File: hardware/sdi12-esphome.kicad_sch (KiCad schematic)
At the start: 24 parts, among them J1 SDI-12 A, J2 SDI-12 B, J3 SDI-12 C, J4 SDI-12 D, J5 Grounding, Q1 2N7002, U1 ESP32_NODEMCU, U2 74LVC1G125, U3 MCP1661

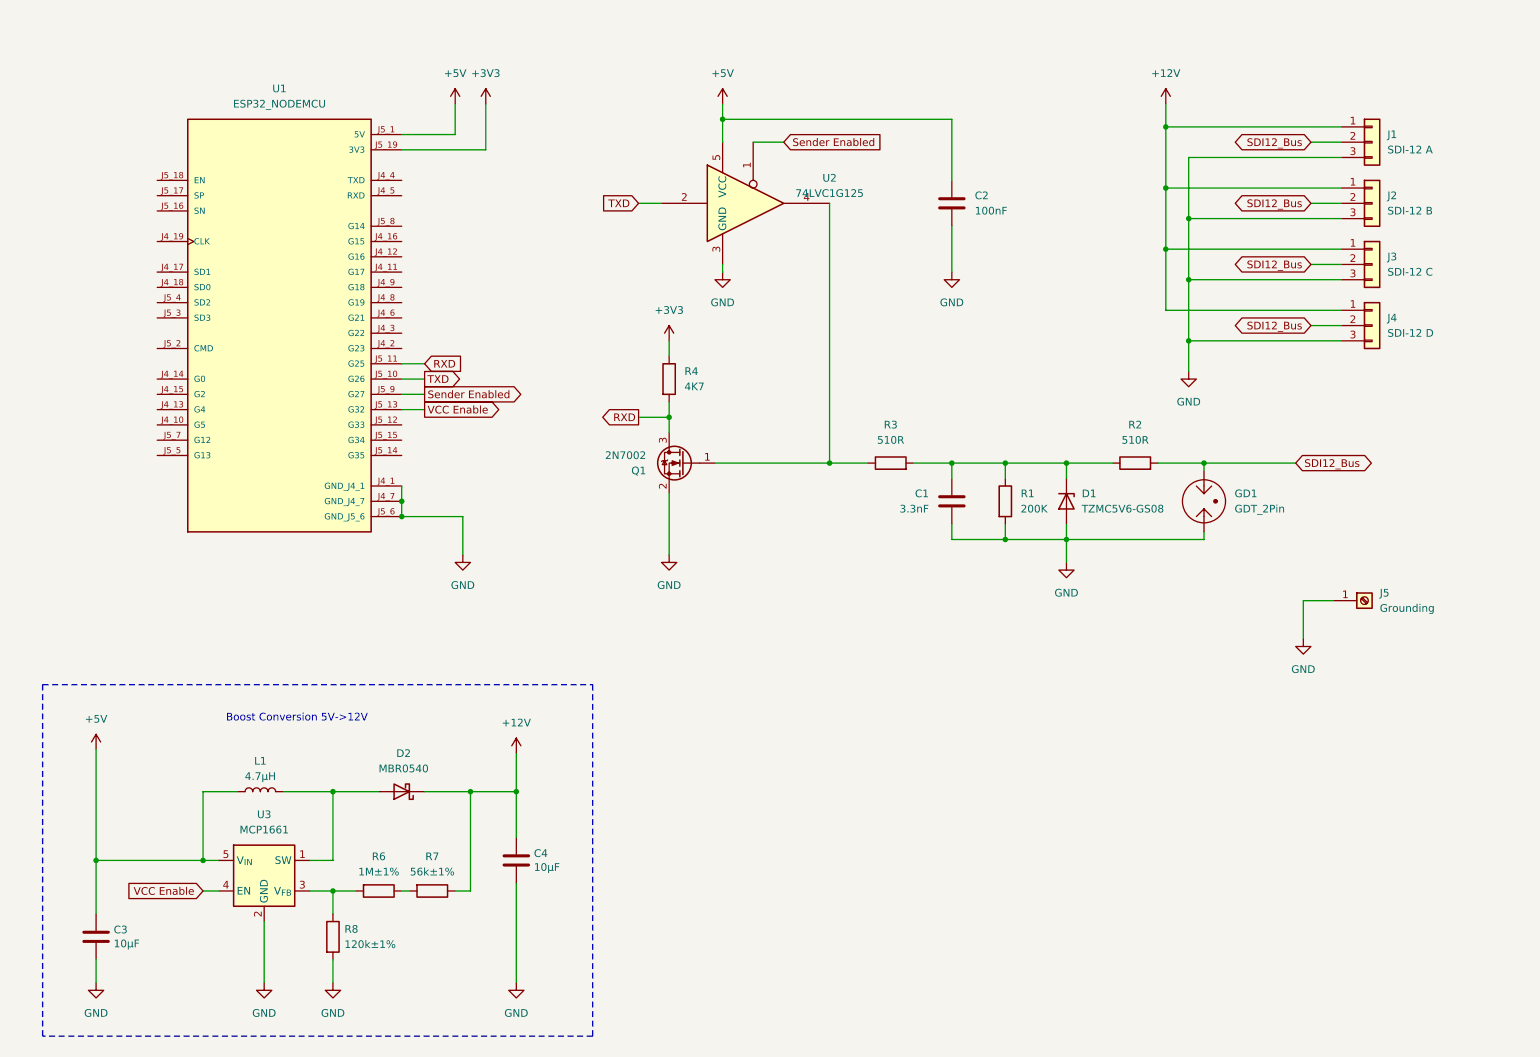
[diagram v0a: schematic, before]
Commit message: Schematic: Add additional GPIO and Rain Gauge ports, re-arrange schematic elements
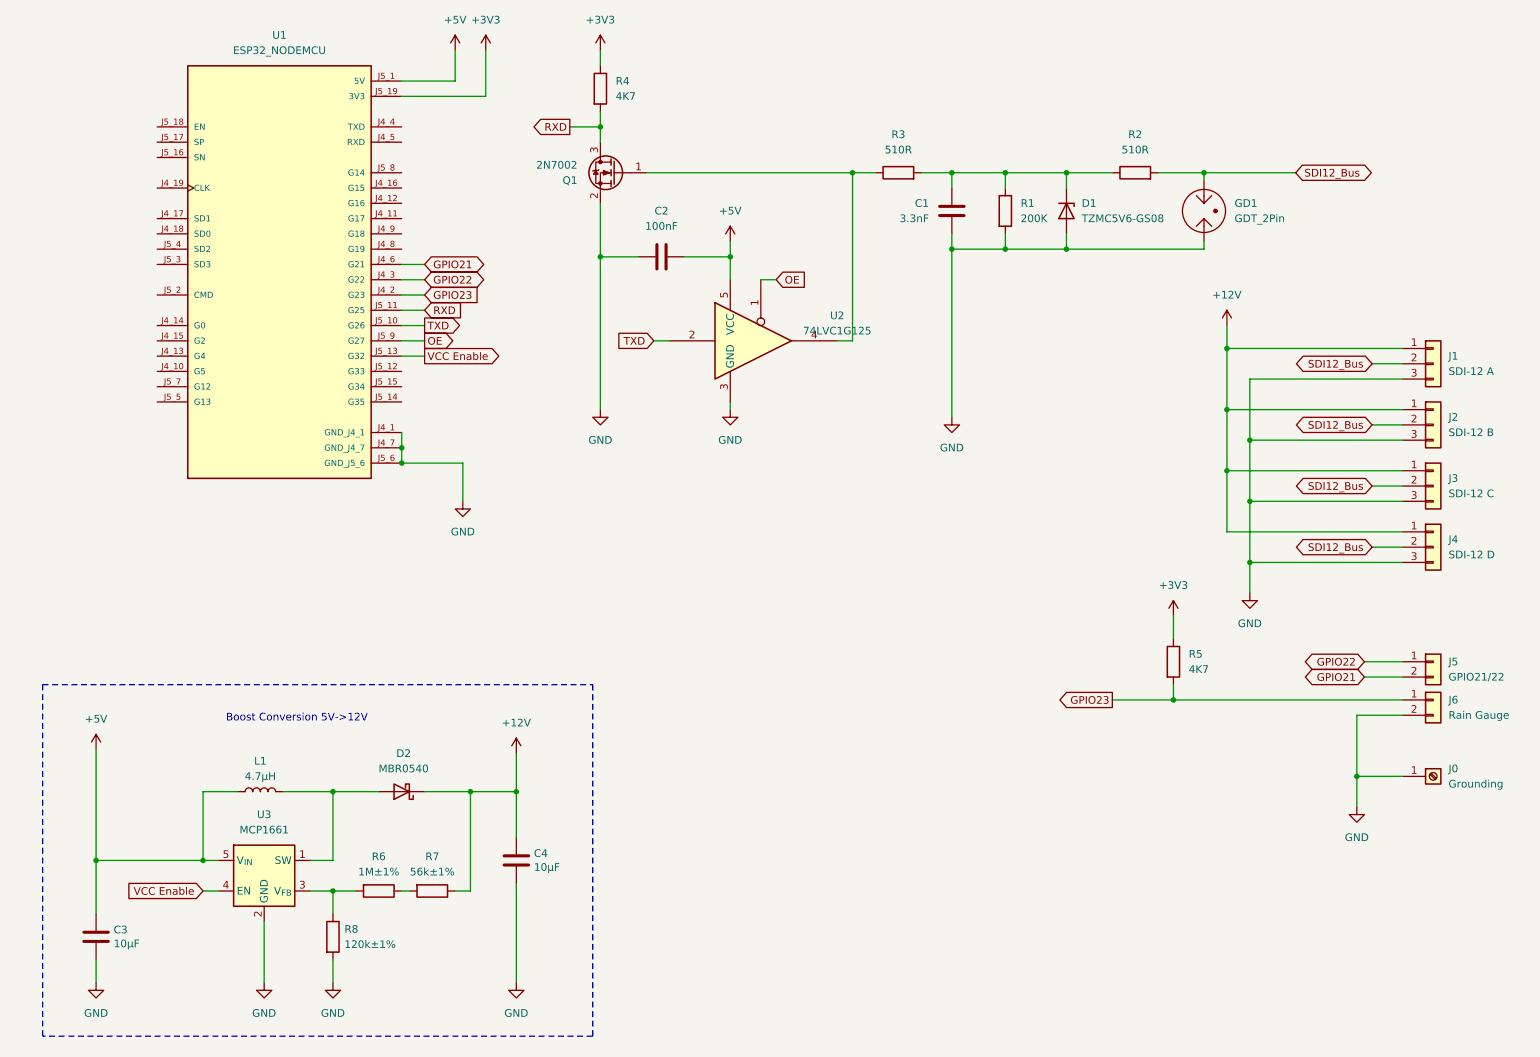
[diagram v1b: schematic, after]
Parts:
- added J5: GPIO21/22, Fraxinas-kicad:Phoenix Contact SPTA 1 2 5,0 1752214, symbol Connector_Generic:Conn_01x02
- added J6: Rain Gauge, Fraxinas-kicad:Phoenix Contact SPTA 1 2 5,0 1752214, symbol Connector_Generic:Conn_01x02
- added R5: 4K7, Resistor_SMD:R_0805_2012Metric_Pad1.20x1.40mm_HandSolder, symbol Device:R
- renumbered J5 to J0
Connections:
- net +3V3: now also R5.1
- net +5V: now also C2.2; no longer C2.1
- net GND: now also C2.1, J6.2 (Pin_2); no longer C2.2
- net GPIO23: now reaches U1.J4_2 (G23)
- net GPIO23: now also J6.1 (Pin_1), R5.2
- net GPIO22: now reaches U1.J4_3 (G22)
- net GPIO22: now also J5.1 (Pin_1)
- net GPIO21: now reaches U1.J4_6 (G21)
- net GPIO21: now also J5.2 (Pin_2)
- net Sender Enabled renamed OE
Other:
- moved on the sheet: C1, C2, D1, GD1, J0, J1, J2, J3, J4, Q1, R1, R2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

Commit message: schematic: Add Bus Power indicator LED, use GD footprint, fix terminal mod
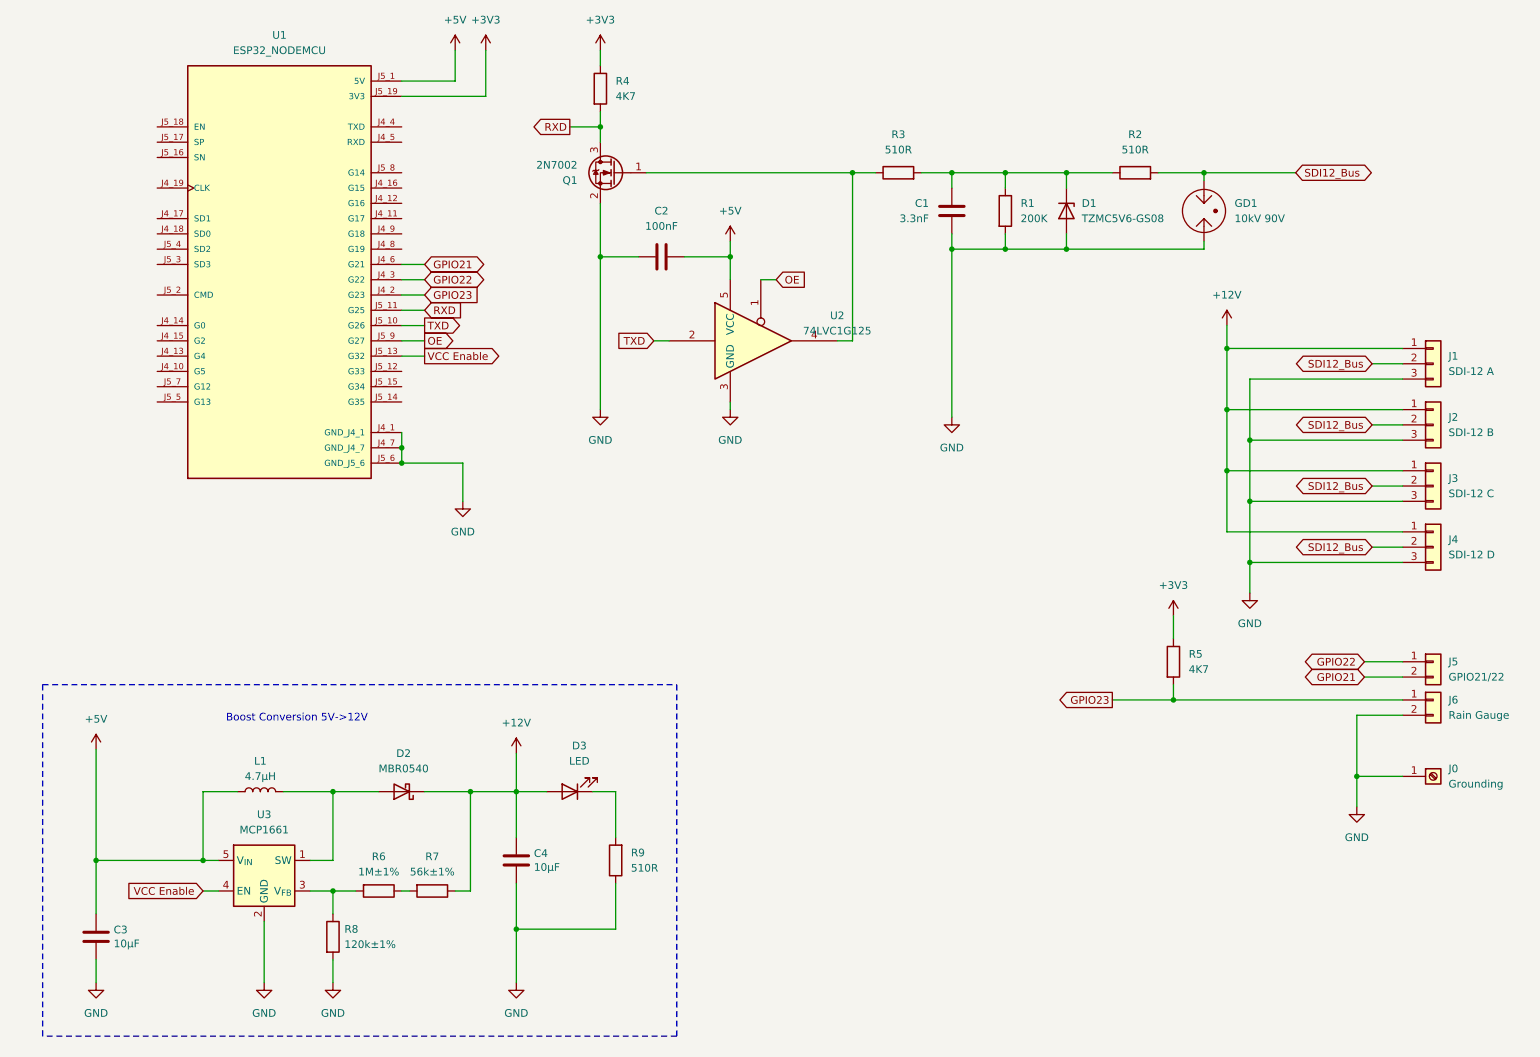
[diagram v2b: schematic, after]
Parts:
- added D3: LED, LED_SMD:LED_0805_2012Metric_Pad1.15x1.40mm_HandSolder, symbol Device:LED
- added R9: 510R, Resistor_SMD:R_0805_2012Metric_Pad1.20x1.40mm_HandSolder, symbol Device:R
- GD1: value GDT_2Pin -> 10kV 90V; footprint Diode_THT:D_P600_R-6_P12.70mm_Horizontal -> Fraxinas-kicad:Gas Discharge Tube Generic 12.7mm THT
- J1, J2, J3, J4: footprint Fraxinas-kicad:Phoenix Contact SPTA 1 3 3,5 1752227 -> Fraxinas-kicad:Phoenix Contact SPTA 1 3 5,0 1752227
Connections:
- net +12V: now also D3.2 (A)
- net GND: now also R9.1
- new net: D3.1 (K), R9.2
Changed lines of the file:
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@@
   (junction (at 186.69 62.23) (diameter 0) (color 0 0 0 0)
   )
+  (junction (at 105.41 175.26) (diameter 0) (color 0 0 0 0)
+  )
   (junction (at 53.34 163.83) (diameter 0) (color 0 0 0 0)
   )
@@
     (stroke (width 0) (type default))
   )
+  (wire (pts (xy 105.41 152.4) (xy 110.49 152.4))
+    (stroke (width 0) (type default))
+  )
   (wire (pts (xy 177.8 62.23) (xy 177.8 90.17))
     (stroke (width 0) (type default))
@@
     (stroke (width 0) (type default))
   )
+  (wire (pts (xy 118.11 152.4) (xy 121.92 152.4))
+    (stroke (width 0) (type default))
+  )
   (wire (pts (xy 186.69 49.53) (xy 196.85 49.53))
     (stroke (width 0) (type default))
@@
     (stroke (width 0) (type default))
   )
+  (wire (pts (xy 105.41 175.26) (xy 105.41 184.15))
+    (stroke (width 0) (type default))
+  )
   (wire (pts (xy 97.79 152.4) (xy 97.79 168.91))
     (stroke (width 0) (type default))
@@
     (stroke (width 0) (type default))
   )
+  (wire (pts (xy 121.92 167.64) (xy 121.92 175.26))
+    (stroke (width 0) (type default))
+  )
   (wire (pts (xy 252.73 99.06) (xy 223.52 99.06))
     (stroke (width 0) (type default))
@@
     (stroke (width 0) (type default))
   )
+  (wire (pts (xy 121.92 152.4) (xy 121.92 160.02))
+    (stroke (width 0) (type default))
+  )
   (wire (pts (xy 219.71 62.23) (xy 219.71 60.96))
     (stroke (width 0) (type default))
@@
     (stroke (width 0) (type default))
   )
+  (wire (pts (xy 121.92 175.26) (xy 105.41 175.26))
+    (stroke (width 0) (type default))
+  )
   (wire (pts (xy 74.93 163.83) (xy 74.93 152.4))
     (stroke (width 0) (type default))
   )
-  (wire (pts (xy 105.41 167.64) (xy 105.41 184.15))
+  (wire (pts (xy 105.41 167.64) (xy 105.41 175.26))
     (stroke (width 0) (type default))
   )
@@
     (stroke (width 0) (type default))
   )
-  (rectangle (start 26.67 134.62) (end 118.11 193.04)
+  (rectangle (start 26.67 134.62) (end 132.08 193.04)
     (stroke (width 0) (type dash))
     (fill (type none))
@@
       (effects (font (size 1.27 1.27)) (justify left))
     )
-    (property "Footprint" "Fraxinas-kicad:Phoenix Contact SPTA 1 3 3,5 1752227" (at 257.81 111.76 0)
+    (property "Footprint" "Fraxinas-kicad:Phoenix Contact SPTA 1 3 5,0 1752227" (at 257.81 111.76 0)
       (effects (font (size 1.27 1.27)) hide)
     )
@@
     )
   )
+  (symbol (lib_id "Device:LED") (at 114.3 152.4 180) (unit 1)
+    (in_bom yes) (on_board yes) (dnp no) (fields_autoplaced)
+    (property "Reference" "D3" (at 115.8875 144.78 0)
+      (effects (font (size 1.27 1.27)))
+    )
+    (property "Value" "LED" (at 115.8875 147.32 0)
+      (effects (font (size 1.27 1.27)))
+    )
+    (property "Footprint" "LED_SMD:LED_0805_2012Metric_Pad1.15x1.40mm_HandSolder" (at 114.3 152.4 0)
+      (effects (font (size 1.27 1.27)) hide)
+    )
+    (property "Datasheet" "~" (at 114.3 152.4 0)
+      (effects (font (size 1.27 1.27)) hide)
+    )
+    (pin "1")
+    (pin "2")
+    (instances
+      (project "sdi12-esphome"
+        (path "/2cd89c3d-735d-4422-af8b-3a5822a68141"
+          (reference "D3") (unit 1)
+        )
+      )
+    )
+  )
   (symbol (lib_id "power:GND") (at 177.8 90.17 0) (unit 1)
     (in_bom yes) (on_board yes) (dnp no)
@@
       (effects (font (size 1.27 1.27)) (justify left))
     )
-    (property "Footprint" "Fraxinas-kicad:Phoenix Contact SPTA 1 3 3,5 1752227" (at 257.81 81.28 0)
+    (property "Footprint" "Fraxinas-kicad:Phoenix Contact SPTA 1 3 5,0 1752227" (at 257.81 81.28 0)
       (effects (font (size 1.27 1.27)) hide)
     )
@@
       (effects (font (size 1.27 1.27)) (justify left))
     )
-    (property "Footprint" "Fraxinas-kicad:Phoenix Contact SPTA 1 3 3,5 1752227" (at 257.81 101.6 0)
+    (property "Footprint" "Fraxinas-kicad:Phoenix Contact SPTA 1 3 5,0 1752227" (at 257.81 101.6 0)
       (effects (font (size 1.27 1.27)) hide)
     )
@@
       (effects (font (size 1.27 1.27)) (justify left))
     )
-    (property "Value" "GDT_2Pin" (at 224.79 57.15 0)
-      (effects (font (size 1.27 1.27)) (justify left))
-    )
-    (property "Footprint" "Diode_THT:D_P600_R-6_P12.70mm_Horizontal" (at 219.71 55.88 90)
+    (property "Value" "10kV 90V" (at 224.79 57.15 0)
+      (effects (font (size 1.27 1.27)) (justify left))
+    )
+    (property "Footprint" "Fraxinas-kicad:Gas Discharge Tube Generic 12.7mm THT" (at 219.71 55.88 90)
       (effects (font (size 1.27 1.27)) hide)
     )
@@
     )
   )
+  (symbol (lib_id "Device:R") (at 121.92 163.83 180) (unit 1)
+    (in_bom yes) (on_board yes) (dnp no) (fields_autoplaced)
+    (property "Reference" "R9" (at 124.46 162.56 0)
+      (effects (font (size 1.27 1.27)) (justify right))
+    )
+    (property "Value" "510R" (at 124.46 165.1 0)
+      (effects (font (size 1.27 1.27)) (justify right))
+    )
+    (property "Footprint" "Resistor_SMD:R_0805_2012Metric_Pad1.20x1.40mm_HandSolder" (at 123.698 163.83 90)
+      (effects (font (size 1.27 1.27)) hide)
+    )
+    (property "Datasheet" "~" (at 121.92 163.83 0)
+      (effects (font (size 1.27 1.27)) hide)
+    )
+    (pin "1")
+    (pin "2")
+    (instances
+      (project "sdi12-esphome"
+        (path "/2cd89c3d-735d-4422-af8b-3a5822a68141"
+          (reference "R9") (unit 1)
+        )
+      )
+    )
+  )
   (symbol (lib_id "power:GND") (at 245.11 154.94 0) (unit 1)
     (in_bom yes) (on_board yes) (dnp no)
@@
       (effects (font (size 1.27 1.27)) (justify left))
     )
-    (property "Footprint" "Fraxinas-kicad:Phoenix Contact SPTA 1 3 3,5 1752227" (at 257.81 91.44 0)
-      (effects (font (size 1.27 1.27)) hide)
-    )
+    (property "Footprint" "Fraxinas-kicad:Phoenix Contact SPTA 1 3 5,0 1752227" (at 257.81 91.44 0)
+      (effects (font (size 1.27 1.27)) hide)
+    )

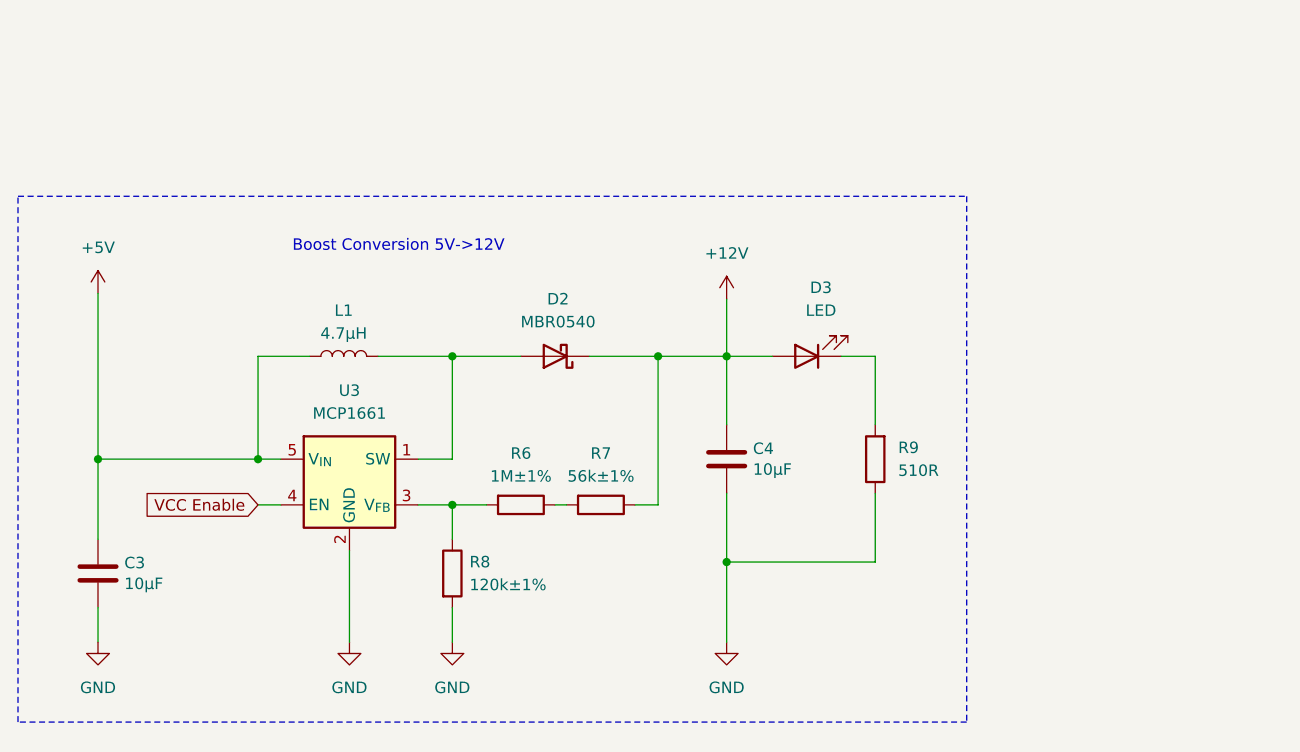
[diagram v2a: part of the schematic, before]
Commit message: Schematic: Add P-MOSFET for power cutoff
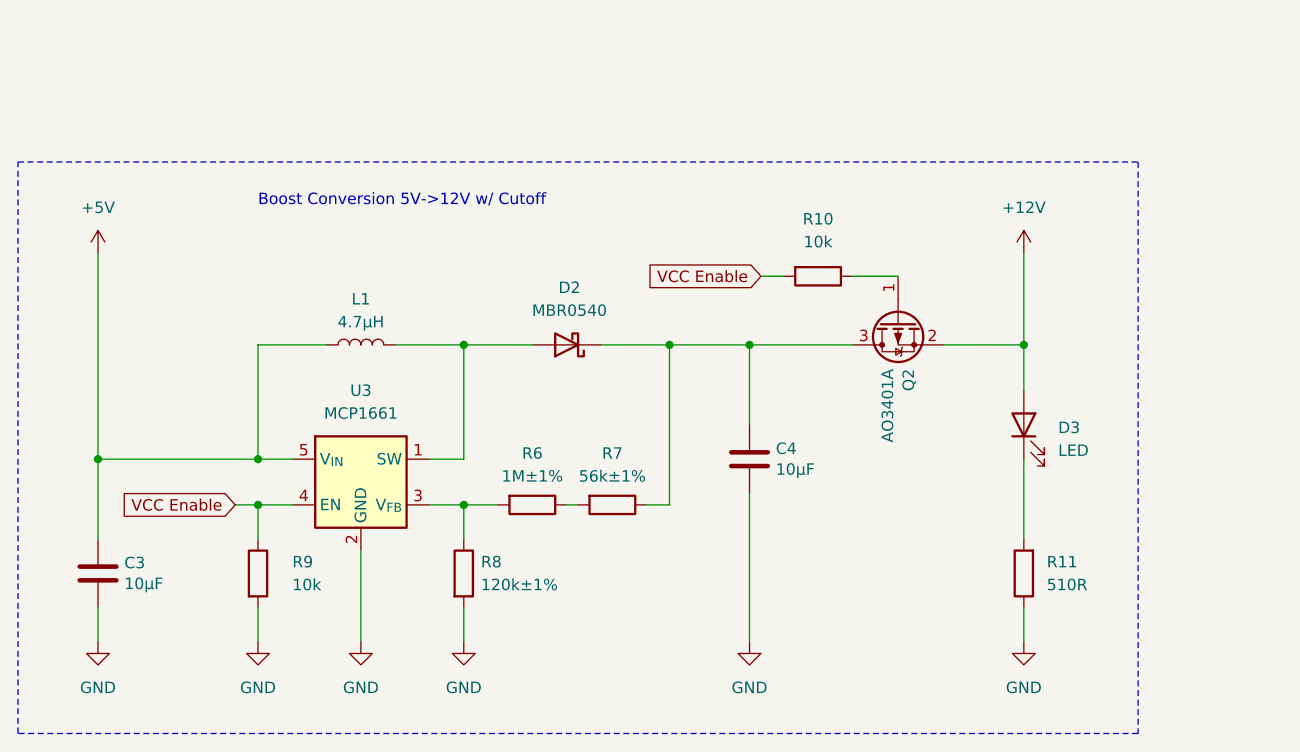
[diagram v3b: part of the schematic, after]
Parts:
- added Q2: AO3401A, Package_TO_SOT_SMD:SOT-23, symbol Transistor_FET:AO3401A
- added R10: 10k, Resistor_SMD:R_0805_2012Metric_Pad1.20x1.40mm_HandSolder, symbol Device:R
- added R11: 510R, Resistor_SMD:R_0805_2012Metric_Pad1.20x1.40mm_HandSolder, symbol Device:R
- R9: value 510R -> 10k
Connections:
- net +12V: now also Q2.2 (S); no longer C4.1, D2.1 (K), R7.1
- net GND: now also R9.2, R11.1; no longer R9.1
- net VCC Enable: now also R9.1, R10.2
- net at D3.1 (K): now also R11.2; no longer R9.2
- new net: C4.1, D2.1 (K), Q2.3 (D), R7.1
- new net: Q2.1 (G), R10.1
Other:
- note added: "Boost Conversion 5V->12V w/ Cutoff"
- note removed: "Boost Conversion 5V->12V"
- moved on the sheet: C4, D2, D3, L1, R6, R7, R8, U3
